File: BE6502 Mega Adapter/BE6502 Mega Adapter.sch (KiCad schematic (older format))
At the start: 12 parts, among them J1 Expansion, J2 Slot #1, J3 Slot #2, M1 Mounting, M2 Mounting, M3 Mounting, M4 Mounting

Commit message: Mega Adapter gerber export
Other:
- note added: "A"
- note added: "The video series uses an Arduino Mega 2560 to monitor the bus signals used by the\ncomputer, this way code can be stepped through (at a low frequency) without the\nuse of a logic analyzer. This module acts as an Arduino shield that maps out all the\nsignals as well as doubling up as a 2/3 slot backplane for your own expansions."
- note removed: "..."
- note removed: "B"
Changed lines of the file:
@@
 $EndComp
 Text Notes 15400 11075 0    60   ~ 0
-B
+A
 Wire Bus Line
 	12625 950  6425 950
@@
 Wire Wire Line
 	12750 4775 12750 4850
-Text Notes 11825 10250 0    60   ~ 0
-...
+Text Notes 11825 10350 0    60   ~ 0
+The video series uses an Arduino Mega 2560 to monitor the bus signals used by the\ncomputer, this way code can be stepped through (at a low frequency) without the\nuse of a logic analyzer. This module acts as an Arduino shield that maps out all the\nsignals as well as doubling up as a 2/3 slot backplane for your own expansions.
 $Comp
 L Arduino_Mega2560_Shield XA1

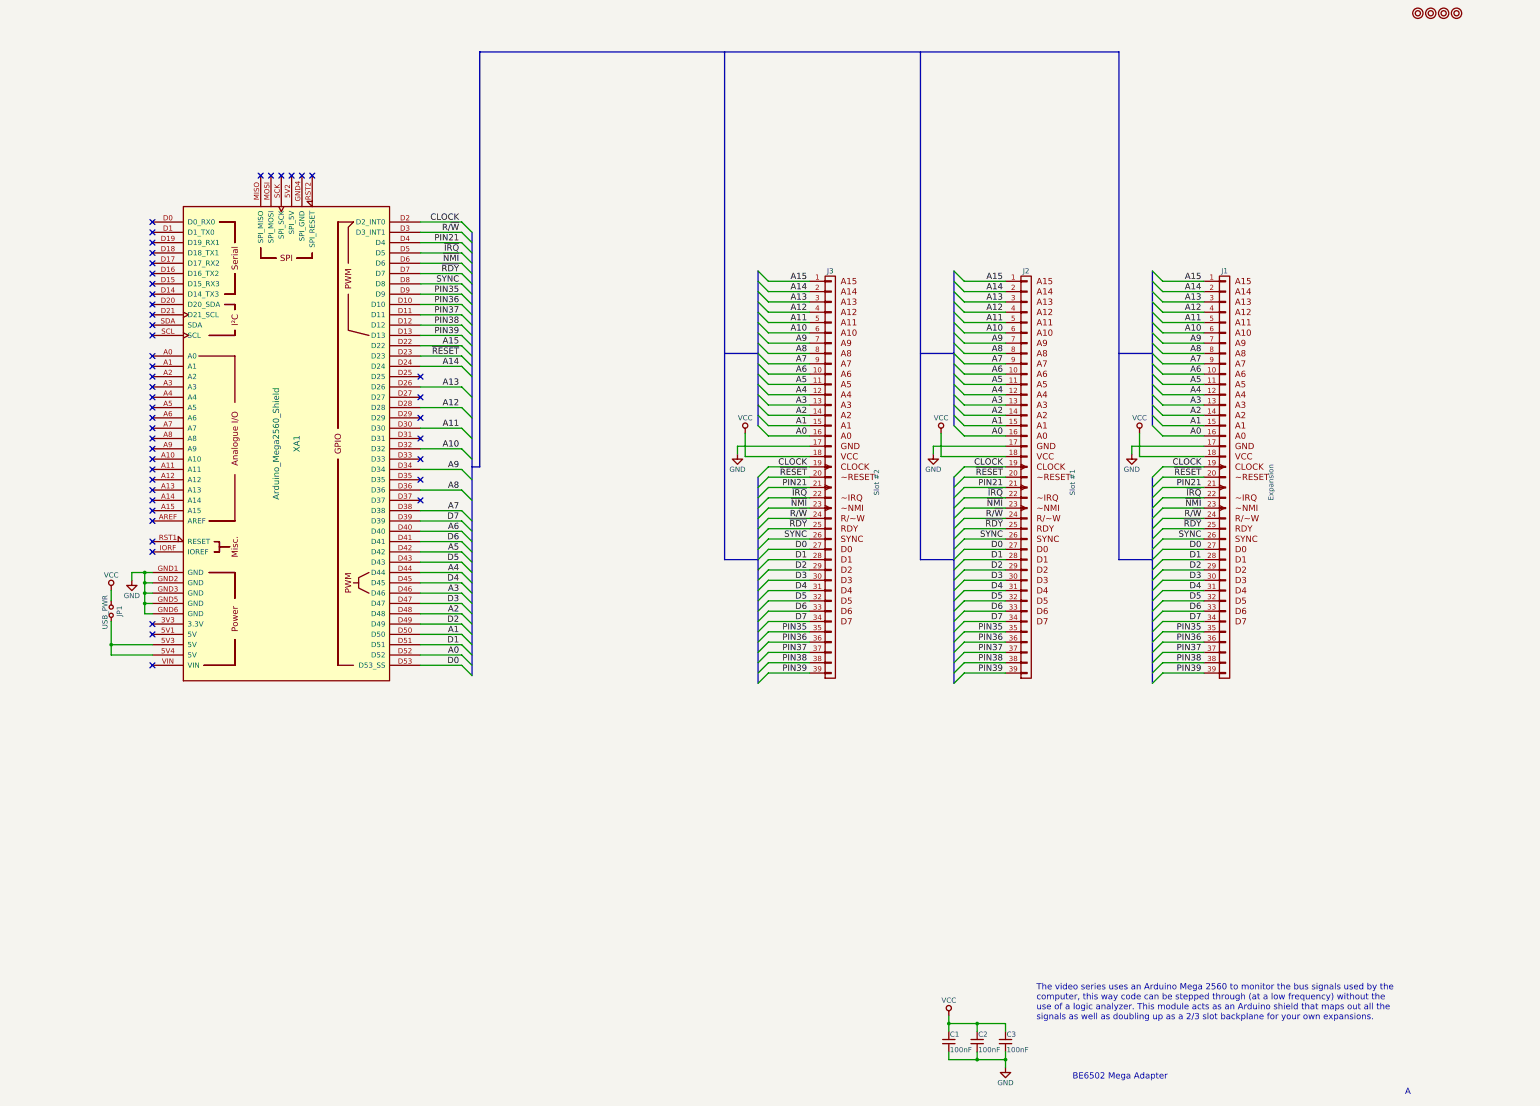
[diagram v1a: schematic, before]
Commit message: Added some switches and an LED to unused pins
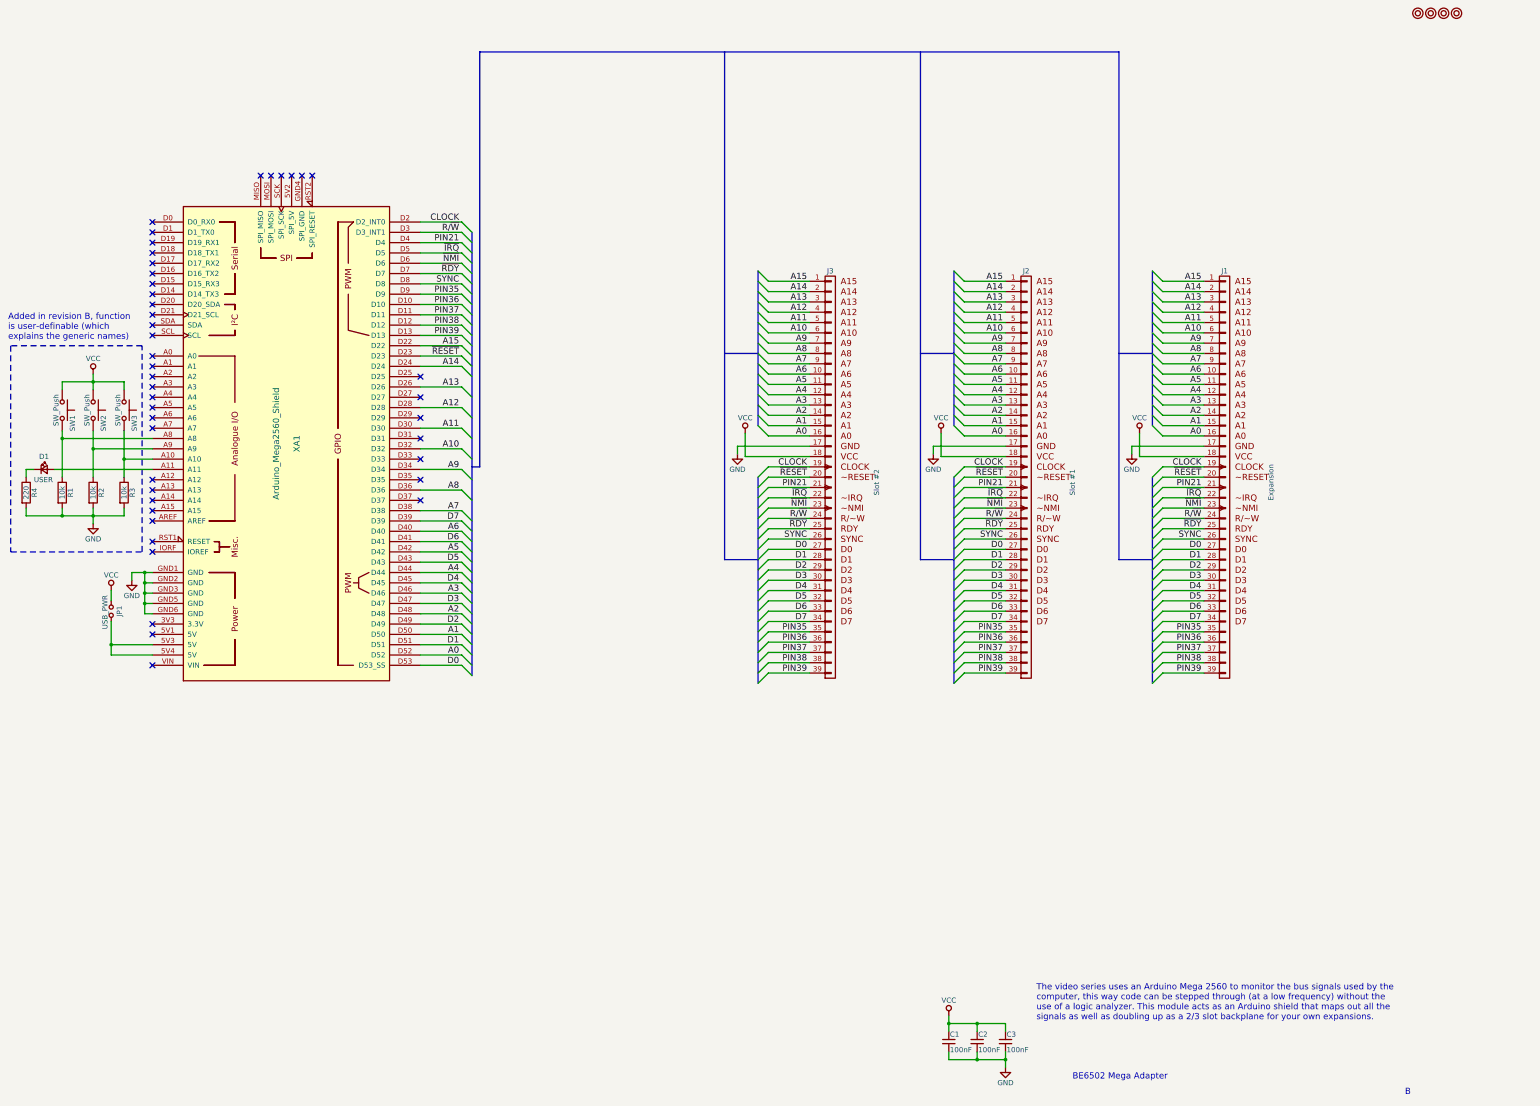
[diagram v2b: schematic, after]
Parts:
- added D1: USER, LEDs:LED_D5.0mm, symbol LED_Small
- added R1, R2, R3: 10k, Resistors_THT:R_Axial_DIN0207_L6.3mm_D2.5mm_P10.16mm_Horizontal, symbol R
- added R4: 220, Resistors_THT:R_Axial_DIN0207_L6.3mm_D2.5mm_P10.16mm_Horizontal, symbol R
- added SW1, SW2, SW3: SW_Push, Buttons_Switches_THT:SW_PUSH_6mm, symbol SW_Push
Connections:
- net GND: now also R1.2, R2.2, R3.2, R4.2
- net VCC: now also SW1.1, SW2.1, SW3.1
- net at XA1.A10: now also R3.1, SW3.2
- net at XA1.A11: now also D1.2 (A)
- net at XA1.A8: now also R1.1, SW1.2
- net at XA1.A9: now also R2.1, SW2.2
- new net: D1.1 (K), R4.1
- no-connect marks 47 -> 43
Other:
- note added: "Added in revision B, function\nis user-definable (which\nexplains the generic names)"
- note added: "B"
- note removed: "A"
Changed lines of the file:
@@
 LIBS:be6502_backplane
 LIBS:arduino
+LIBS:switches
 LIBS:BE6502 Mega Adapter-cache
 EELAYER 25 0
@@
 $EndComp
 Text Notes 15400 11075 0    60   ~ 0
-A
+B
 Wire Bus Line
 	12625 950  6425 950
@@
 NoConn ~ 3250 3600
 NoConn ~ 3250 3700
-NoConn ~ 3250 3900
-NoConn ~ 3250 4000
-NoConn ~ 3250 4100
-NoConn ~ 3250 4200
 NoConn ~ 3250 4300
 NoConn ~ 3250 4400
 NoConn ~ 3250 4500
 NoConn ~ 3250 4600
-NoConn ~ 3250 4700
-NoConn ~ 3250 4800
-NoConn ~ 3250 4900
-NoConn ~ 3250 5000
 NoConn ~ 3250 5100
 NoConn ~ 3250 5200
@@
 	6250 3900 6350 4000
 NoConn ~ 3250 6600
+$Comp
+L SW_Push SW1
+U 1 1 5E236342
+P 2375 4425
+F 0 "SW1" H 2425 4525 50  0000 L CNN
+F 1 "SW_Push" H 2375 4365 50  0000 C CNN
+F 2 "Buttons_Switches_THT:SW_PUSH_6mm" H 2375 4625 50  0001 C CNN
+F 3 "" H 2375 4625 50  0001 C CNN
+	1    2375 4425
+	0    1    1    0
+$EndComp
+$Comp
+L R R1
+U 1 1 5E2364BC
+P 2375 5225
+F 0 "R1" V 2455 5225 50  0000 C CNN
+F 1 "10k" V 2375 5225 50  0000 C CNN
+F 2 "Resistors_THT:R_Axial_DIN0207_L6.3mm_D2.5mm_P10.16mm_Horizontal" V 2305 5225 50  0001 C CNN
+F 3 "" H 2375 5225 50  0001 C CNN
+	1    2375 5225
+	1    0    0    -1
+$EndComp
+$Comp
+L R R2
+U 1 1 5E2366D0
+P 2675 5225
+F 0 "R2" V 2755 5225 50  0000 C CNN
+F 1 "10k" V 2675 5225 50  0000 C CNN
+F 2 "Resistors_THT:R_Axial_DIN0207_L6.3mm_D2.5mm_P10.16mm_Horizontal" V 2605 5225 50  0001 C CNN
+F 3 "" H 2675 5225 50  0001 C CNN
+	1    2675 5225
+	1    0    0    -1
+$EndComp
+$Comp
+L R R3
+U 1 1 5E236709
+P 2975 5225
+F 0 "R3" V 3055 5225 50  0000 C CNN
+F 1 "10k" V 2975 5225 50  0000 C CNN
+F 2 "Resistors_THT:R_Axial_DIN0207_L6.3mm_D2.5mm_P10.16mm_Horizontal" V 2905 5225 50  0001 C CNN
+F 3 "" H 2975 5225 50  0001 C CNN
+	1    2975 5225
+	1    0    0    -1
+$EndComp
+$Comp
+L SW_Push SW2
+U 1 1 5E2369FB
+P 2675 4425
+F 0 "SW2" H 2725 4525 50  0000 L CNN
+F 1 "SW_Push" H 2675 4365 50  0000 C CNN
+F 2 "Buttons_Switches_THT:SW_PUSH_6mm" H 2675 4625 50  0001 C CNN
+F 3 "" H 2675 4625 50  0001 C CNN
+	1    2675 4425
+	0    1    1    0
+$EndComp
+$Comp
+L SW_Push SW3
+U 1 1 5E236B4B
+P 2975 4425
+F 0 "SW3" H 3025 4525 50  0000 L CNN
+F 1 "SW_Push" H 2975 4365 50  0000 C CNN
+F 2 "Buttons_Switches_THT:SW_PUSH_6mm" H 2975 4625 50  0001 C CNN
+F 3 "" H 2975 4625 50  0001 C CNN
+	1    2975 4425
+	0    1    1    0
+$EndComp
+Wire Wire Line
+	2375 4625 2375 5075
+Wire Wire Line
+	3250 4700 2375 4700
+Connection ~ 2375 4700
+Wire Wire Line
+	2675 4625 2675 5075
+Wire Wire Line
+	2675 4800 3250 4800
+Connection ~ 2675 4800
+Wire Wire Line
+	3250 4900 2975 4900
+Wire Wire Line
+	2975 4625 2975 5075
+Connection ~ 2975 4900
+Wire Wire Line
+	2375 5375 2375 5450
+Wire Wire Line
+	2025 5450 2975 5450
+Wire Wire Line
+	2975 5450 2975 5375
+Wire Wire Line
+	2675 5375 2675 5525
+Connection ~ 2675 5450
+Wire Wire Line
+	2375 4225 2375 4150
+Wire Wire Line
+	2375 4150 2975 4150
+Wire Wire Line
+	2975 4150 2975 4225
+Wire Wire Line
+	2675 4075 2675 4225
+Connection ~ 2675 4150
+$Comp
+L VCC #PWR011
+U 1 1 5E237AFB
+P 2675 4075
+F 0 "#PWR011" H 2675 3925 50  0001 C CNN
+F 1 "VCC" H 2675 4225 50  0000 C CNN
+F 2 "" H 2675 4075 50  0001 C CNN
+F 3 "" H 2675 4075 50  0001 C CNN
+	1    2675 4075
+	1    0    0    -1
+$EndComp
+$Comp
+L GND #PWR012
+U 1 1 5E237B2B
+P 2675 5525
+F 0 "#PWR012" H 2675 5275 50  0001 C CNN
+F 1 "GND" H 2675 5375 50  0000 C CNN
+F 2 "" H 2675 5525 50  0001 C CNN
+F 3 "" H 2675 5525 50  0001 C CNN
+	1    2675 5525
+	1    0    0    -1
+$EndComp
+$Comp
+L LED_Small D1
+U 1 1 5E2392BC
+P 2200 5000
+F 0 "D1" H 2150 5125 50  0000 L CNN
+F 1 "USER" H 2100 4900 50  0000 L CNN
+F 2 "LEDs:LED_D5.0mm" V 2200 5000 50  0001 C CNN
+F 3 "" V 2200 5000 50  0001 C CNN
+	1    2200 5000
+	1    0    0    -1
+$EndComp
+Wire Wire Line
+	3250 5000 2300 5000
+$Comp
+L R R4
+U 1 1 5E239C19
+P 2025 5225
+F 0 "R4" V 2105 5225 50  0000 C CNN
+F 1 "220" V 2025 5225 50  0000 C CNN
+F 2 "Resistors_THT:R_Axial_DIN0207_L6.3mm_D2.5mm_P10.16mm_Horizontal" V 1955 5225 50  0001 C CNN
+F 3 "" H 2025 5225 50  0001 C CNN
+	1    2025 5225
+	1    0    0    -1
+$EndComp
+Wire Wire Line
+	2025 5075 2025 5000
+Wire Wire Line
+	2025 5000 2100 5000
+Wire Wire Line
+	2025 5375 2025 5450
+Connection ~ 2375 5450
+NoConn ~ 3250 3900
+NoConn ~ 3250 4000
+NoConn ~ 3250 4100
+NoConn ~ 3250 4200
+Wire Notes Line
+	3150 5800 3150 3800
+Wire Notes Line
+	3150 3800 1875 3800
+Wire Notes Line
+	1875 3800 1875 5800
+Wire Notes Line
+	1875 5800 3150 5800
+Text Notes 1850 3750 0    60   ~ 0
+Added in revision B, function\nis user-definable (which\nexplains the generic names)
 $EndSCHEMATC
